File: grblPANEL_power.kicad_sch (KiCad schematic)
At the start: 26 parts, among them J101 Conn_01x02, U101 MAX17612A, U102 AZ1117-3.3

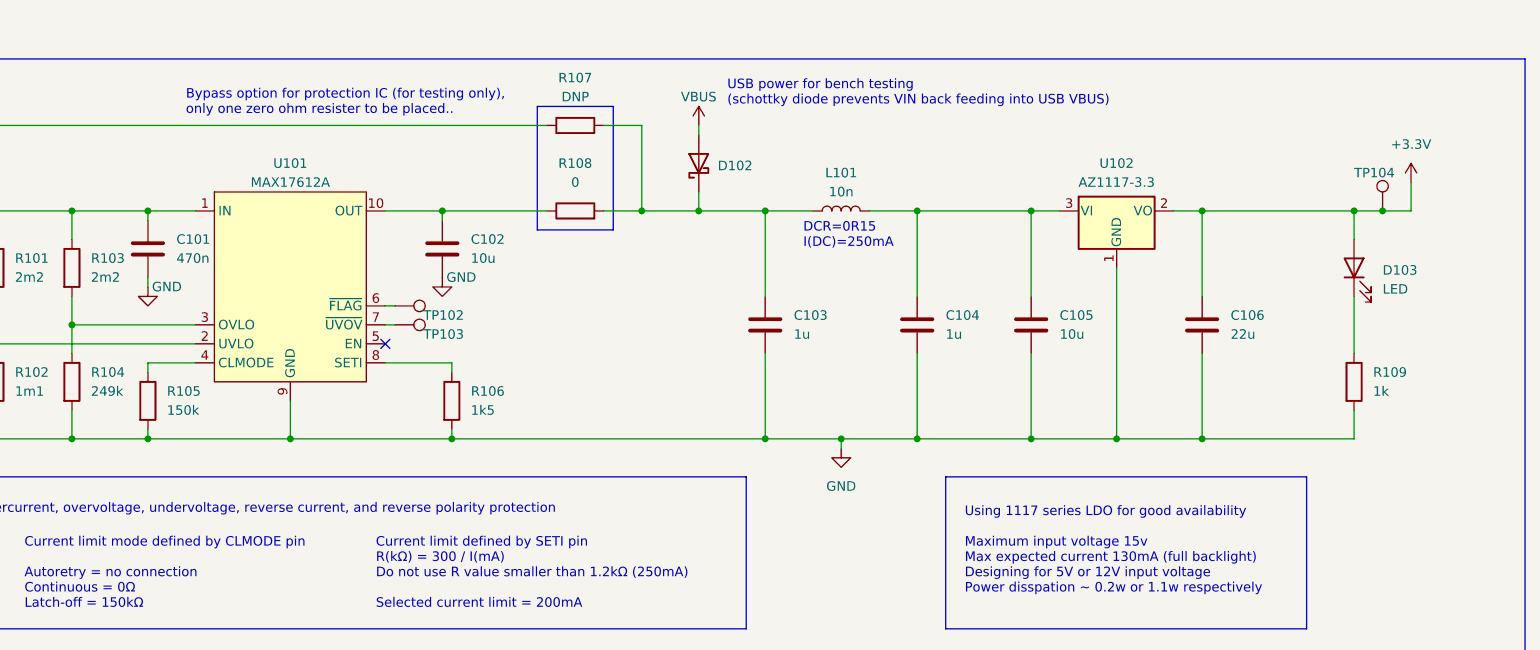
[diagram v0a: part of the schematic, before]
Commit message: ERC fixes
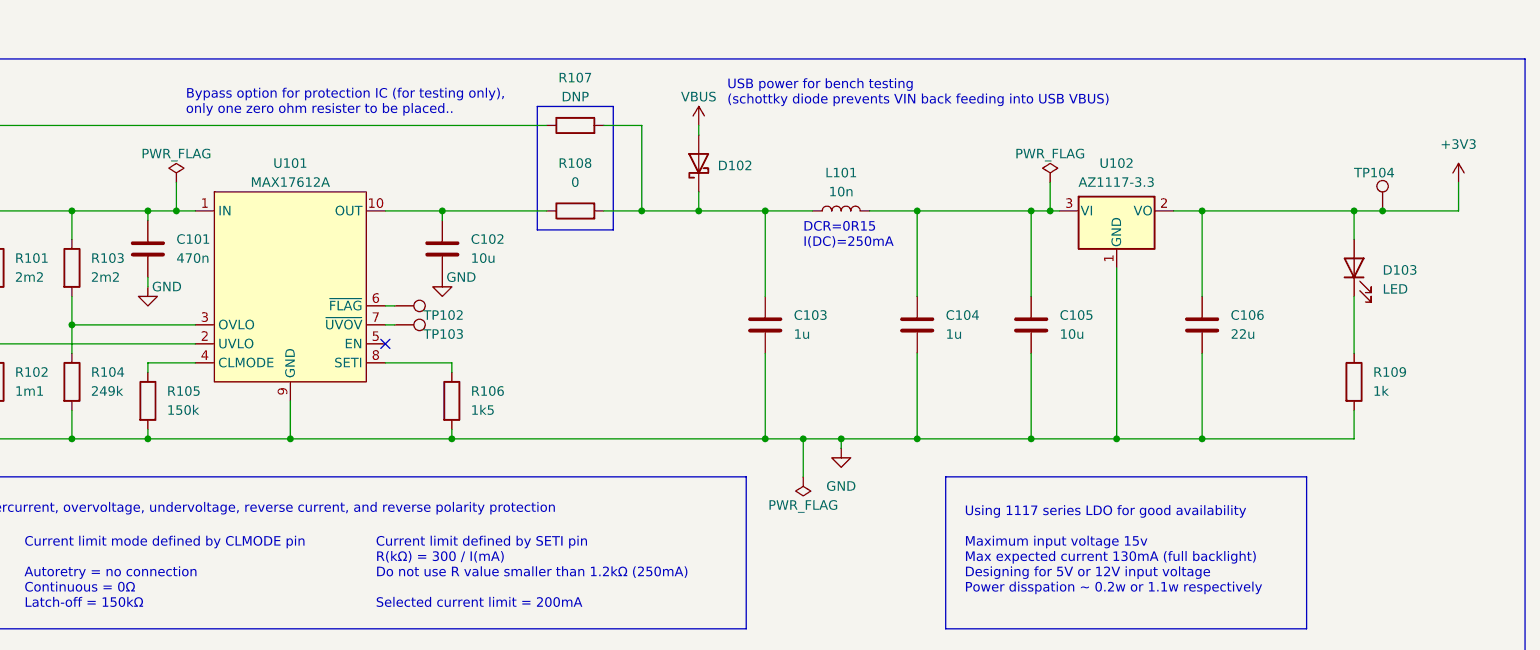
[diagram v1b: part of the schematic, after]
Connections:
- net +3.3V renamed +3V3
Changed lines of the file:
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@@
   (junction (at 77.47 80.01) (diameter 0) (color 0 0 0 0)
   )
+  (junction (at 91.44 64.77) (diameter 0) (color 0 0 0 0)
+  )
   (junction (at 77.47 95.25) (diameter 0) (color 0 0 0 0)
   )
@@
   (junction (at 228.6 64.77) (diameter 0) (color 0 0 0 0)
   )
+  (junction (at 175.26 95.25) (diameter 0) (color 0 0 0 0)
+  )
   (junction (at 127 64.77) (diameter 0) (color 0 0 0 0)
   )
@@
   )
   (junction (at 128.27 95.25) (diameter 0) (color 0 0 0 0)
+  )
+  (junction (at 208.28 64.77) (diameter 0) (color 0 0 0 0)
   )
   (junction (at 217.17 95.25) (diameter 0) (color 0 0 0 0)
@@
     (stroke (width 0) (type default) (color 0 0 0 0))
   )
-  (wire (pts (xy 87.63 64.77) (xy 93.98 64.77))
+  (wire (pts (xy 208.28 64.77) (xy 205.74 64.77))
+    (stroke (width 0) (type default) (color 0 0 0 0))
+  )
+  (wire (pts (xy 87.63 64.77) (xy 91.44 64.77))
     (stroke (width 0) (type default) (color 0 0 0 0))
   )
@@
     (stroke (width 0) (type default) (color 0 0 0 0))
   )
-  (wire (pts (xy 209.55 64.77) (xy 205.74 64.77))
+  (wire (pts (xy 209.55 64.77) (xy 208.28 64.77))
+    (stroke (width 0) (type default) (color 0 0 0 0))
+  )
+  (wire (pts (xy 208.28 60.96) (xy 208.28 64.77))
     (stroke (width 0) (type default) (color 0 0 0 0))
   )
@@
     (stroke (width 0) (type default) (color 0 0 0 0))
   )
+  (wire (pts (xy 91.44 60.96) (xy 91.44 64.77))
+    (stroke (width 0) (type default) (color 0 0 0 0))
+  )
   (wire (pts (xy 46.99 64.77) (xy 50.8 64.77))
     (stroke (width 0) (type default) (color 0 0 0 0))
@@
     (stroke (width 0) (type default) (color 0 0 0 0))
   )
+  (wire (pts (xy 224.79 64.77) (xy 228.6 64.77))
+    (stroke (width 0) (type default) (color 0 0 0 0))
+  )
   (wire (pts (xy 248.92 64.77) (xy 248.92 68.58))
     (stroke (width 0) (type default) (color 0 0 0 0))
   )
+  (wire (pts (xy 175.26 95.25) (xy 175.26 100.33))
+    (stroke (width 0) (type default) (color 0 0 0 0))
+  )
+  (wire (pts (xy 170.18 95.25) (xy 175.26 95.25))
+    (stroke (width 0) (type default) (color 0 0 0 0))
+  )
   (wire (pts (xy 67.31 64.77) (xy 77.47 64.77))
     (stroke (width 0) (type default) (color 0 0 0 0))
@@
     (stroke (width 0) (type default) (color 0 0 0 0))
   )
-  (wire (pts (xy 256.54 64.77) (xy 252.73 64.77))
+  (wire (pts (xy 262.89 64.77) (xy 252.73 64.77))
     (stroke (width 0) (type default) (color 0 0 0 0))
   )
@@
     (stroke (width 0) (type default) (color 0 0 0 0))
   )
-  (wire (pts (xy 248.92 64.77) (xy 228.6 64.77))
-    (stroke (width 0) (type default) (color 0 0 0 0))
-  )
   (wire (pts (xy 148.59 53.34) (xy 153.67 53.34))
     (stroke (width 0) (type default) (color 0 0 0 0))
@@
     (stroke (width 0) (type default) (color 0 0 0 0))
   )
-  (wire (pts (xy 256.54 60.96) (xy 256.54 64.77))
+  (wire (pts (xy 262.89 60.96) (xy 262.89 64.77))
     (stroke (width 0) (type default) (color 0 0 0 0))
   )
@@
     (stroke (width 0) (type default) (color 0 0 0 0))
   )
+  (wire (pts (xy 175.26 95.25) (xy 180.34 95.25))
+    (stroke (width 0) (type default) (color 0 0 0 0))
+  )
   (polyline (pts (xy 25.4 44.45) (xy 25.4 124.46))
     (stroke (width 0) (type default) (color 0 0 0 0))
   )
+  (wire (pts (xy 228.6 64.77) (xy 248.92 64.77))
+    (stroke (width 0) (type default) (color 0 0 0 0))
+  )
   (wire (pts (xy 127 64.77) (xy 140.97 64.77))
     (stroke (width 0) (type default) (color 0 0 0 0))
@@
     (stroke (width 0) (type default) (color 0 0 0 0))
   )
-  (wire (pts (xy 224.79 64.77) (xy 228.6 64.77))
-    (stroke (width 0) (type default) (color 0 0 0 0))
-  )
   (wire (pts (xy 228.6 64.77) (xy 228.6 76.2))
     (stroke (width 0) (type default) (color 0 0 0 0))
@@
     (stroke (width 0) (type default) (color 0 0 0 0))
   )
+  (wire (pts (xy 91.44 64.77) (xy 93.98 64.77))
+    (stroke (width 0) (type default) (color 0 0 0 0))
+  )
   (wire (pts (xy 87.63 73.66) (xy 87.63 74.93))
     (stroke (width 0) (type default) (color 0 0 0 0))
   )
   (wire (pts (xy 67.31 64.77) (xy 67.31 68.58))
-    (stroke (width 0) (type default) (color 0 0 0 0))
-  )
-  (wire (pts (xy 170.18 95.25) (xy 180.34 95.25))
     (stroke (width 0) (type default) (color 0 0 0 0))
   )
@@
     (pin "1")
   )
+  (symbol (lib_id "power:+3V3") (at 262.89 60.96 0) (unit 1)
+    (in_bom yes) (on_board yes) (fields_autoplaced)
+    (property "Reference" "#PWR0106" (id 0) (at 262.89 64.77 0)
+      (effects (font (size 1.27 1.27)) hide)
+    )
+    (property "Value" "+3V3" (id 1) (at 262.89 55.88 0))
+    (property "Footprint" "" (id 2) (at 262.89 60.96 0)
+      (effects (font (size 1.27 1.27)) hide)
+    )
+    (property "Datasheet" "" (id 3) (at 262.89 60.96 0)
+      (effects (font (size 1.27 1.27)) hide)
+    )
+    (pin "1")
+  )
   (symbol (lib_id "Device:C") (at 170.18 80.01 0) (unit 1)
     (in_bom yes) (on_board yes)
@@
     (pin "1")
     (pin "2")
-  )
-  (symbol (lib_id "power:+3.3V") (at 256.54 60.96 0) (unit 1)
-    (in_bom yes) (on_board yes) (fields_autoplaced)
-    (property "Reference" "#PWR0106" (id 0) (at 256.54 64.77 0)
-      (effects (font (size 1.27 1.27)) hide)
-    )
-    (property "Value" "+3.3V" (id 1) (at 256.54 55.88 0))
-    (property "Footprint" "" (id 2) (at 256.54 60.96 0)
-      (effects (font (size 1.27 1.27)) hide)
-    )
-    (property "Datasheet" "" (id 3) (at 256.54 60.96 0)
-      (effects (font (size 1.27 1.27)) hide)
-    )
-    (pin "1")
   )
   (symbol (lib_id "power:VBUS") (at 161.29 53.34 0) (unit 1)
@@
     )
     (property "Datasheet" "" (id 3) (at 46.99 60.96 0)
+      (effects (font (size 1.27 1.27)) hide)
+    )
+    (pin "1")
+  )
+  (symbol (lib_id "power:PWR_FLAG") (at 91.44 60.96 0) (unit 1)
+    (in_bom yes) (on_board yes)
+    (property "Reference" "#FLG0101" (id 0) (at 91.44 59.055 0)
+      (effects (font (size 1.27 1.27)) hide)
+    )
+    (property "Value" "PWR_FLAG" (id 1) (at 91.44 57.15 0))
+    (property "Footprint" "" (id 2) (at 91.44 60.96 0)
+      (effects (font (size 1.27 1.27)) hide)
+    )
+    (property "Datasheet" "~" (id 3) (at 91.44 60.96 0)
       (effects (font (size 1.27 1.27)) hide)
     )
@@
     (pin "2")
   )
+  (symbol (lib_id "power:PWR_FLAG") (at 175.26 100.33 0) (mirror x) (unit 1)
+    (in_bom yes) (on_board yes)
+    (property "Reference" "#FLG0104" (id 0) (at 175.26 102.235 0)
+      (effects (font (size 1.27 1.27)) hide)
+    )
+    (property "Value" "PWR_FLAG" (id 1) (at 175.26 104.14 0))
+    (property "Footprint" "" (id 2) (at 175.26 100.33 0)
+      (effects (font (size 1.27 1.27)) hide)
+    )
+    (property "Datasheet" "~" (id 3) (at 175.26 100.33 0)
+      (effects (font (size 1.27 1.27)) hide)
+    )
+    (pin "1")
+  )
+  (symbol (lib_id "power:PWR_FLAG") (at 208.28 60.96 0) (unit 1)
+    (in_bom yes) (on_board yes)
+    (property "Reference" "#FLG0103" (id 0) (at 208.28 59.055 0)
+      (effects (font (size 1.27 1.27)) hide)
+    )
+    (property "Value" "PWR_FLAG" (id 1) (at 208.28 57.15 0))
+    (property "Footprint" "" (id 2) (at 208.28 60.96 0)
+      (effects (font (size 1.27 1.27)) hide)
+    )
+    (property "Datasheet" "~" (id 3) (at 208.28 60.96 0)
+      (effects (font (size 1.27 1.27)) hide)
+    )
+    (pin "1")
+  )
   (symbol (lib_id "Device:R") (at 144.78 53.34 90) (unit 1)

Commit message: Refresh
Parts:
- added TP104: TestPoint, Connector_Pin:Pin_D1.0mm_L10.0mm, symbol Connector:TestPoint
- C101: footprint (none) -> Capacitor_SMD:C_0805_2012Metric
- C102, C105, C106: footprint (none) -> Capacitor_SMD:C_1206_3216Metric
- C103, C104: footprint (none) -> Capacitor_SMD:C_0603_1608Metric
- D101: footprint (none) -> Diode_SMD:D_SMA
- D102: footprint (none) -> Diode_SMD:D_SOD-323
- D103: footprint (none) -> LED_SMD:LED_0603_1608Metric
- J101: footprint (none) -> TerminalBlock_4Ucon:TerminalBlock_4Ucon_1x02_P3.50mm_Horizontal
- L101: footprint (none) -> Inductor_SMD:L_0603_1608Metric
- R101, R102, R103, R104, R105, R106, R107, R108, R109: footprint (none) -> Resistor_SMD:R_0603_1608Metric
- TP101: footprint (none) -> Connector_Pin:Pin_D1.0mm_L10.0mm_LooseFit
- TP102, TP103: footprint (none) -> Connector_Pin:Pin_D1.0mm_L10.0mm
- TP105: renamed from TP104; footprint (none) -> Connector_Pin:Pin_D1.0mm_L10.0mm
- U101: footprint (none) -> Package_DFN_QFN:TDFN-10-1EP_2x3mm_P0.5mm_EP0.9x2mm_ThermalVias
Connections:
- net GND: now also TP104.1
